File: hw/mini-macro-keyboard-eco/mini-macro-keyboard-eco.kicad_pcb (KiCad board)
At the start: 2 copper layers, 59.2 x 30.5 mm, 32 parts, among them J0 USB, J1 DEBUG_SWD, SW1 SW_Cherry_MX_1.00u_PCB, SW2 SW_Cherry_MX_1.00u_PCB, SW3 SW_Cherry_MX_1.00u_PCB, SW5 LAYOUT, SW6 BACKLIGHT, U1 USBLC6-2SC6, U2 XC6206P322MR, U3 STM32F070F6P6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

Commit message: fix(hw): reroute some traces
Signed-off-by: Ivan Kovalenko <s1ckretbox@gmail.com>
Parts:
- moved C0 4.99 mm to (125.1, 112.6)
- moved C1 4.11 mm to (127.3, 109.9), turned to 0 degrees
- moved R0 2.35 mm to (130.1, 111.4)
- moved Y1 0.54 mm to (127.3, 112.5), turned to 90 degrees
- moved R2 0.09 mm to (143.3, 105.1)
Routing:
- net GND: track 30.6 -> 48.8 mm, vias 10 -> 12
- net Net-(J0-Pad6): track 0.00 -> 12.4 mm
- net USB_D-: track 22.1 -> 27.4 mm
- net USB_D+: track 22.9 -> 28.1 mm
- net OSC_IN: track 4.72 -> 7.76 mm
- net OSC_OUT: track 4.25 -> 1.27 mm
- net +3V3: track 18.2 -> 21.2 mm, vias 4 -> 6
- net Net-(C1-Pad2): track 3.75 -> 3.18 mm
- net SWCLK: vias 0 -> 1

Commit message: fix(hw, #3): remove R0 resistor
Signed-off-by: Ivan Kovalenko <s1ckretbox@gmail.com>
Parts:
- removed R0: 47, Resistor_SMD:R_0402_1005Metric
- moved Y1 2.28 mm to (129.5, 112.0)
- moved C0 2.13 mm to (127.2, 112.6)
- moved C1 1.94 mm to (129.1, 109.2)
- moved C3 1.44 mm to (130.7, 108.6), turned to 90 degrees
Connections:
- C1 pad 2: Net-(C1-Pad2) -> OSC_OUT
- Y1 pad 3: Net-(C1-Pad2) -> OSC_OUT
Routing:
- net GND: track 48.8 -> 42.7 mm, vias 12 -> 11
- net Net-(C1-Pad2): track 3.18 -> 0.00 mm
- net OSC_OUT: track 1.27 -> 4.22 mm
- net OSC_IN: track 7.76 -> 6.25 mm

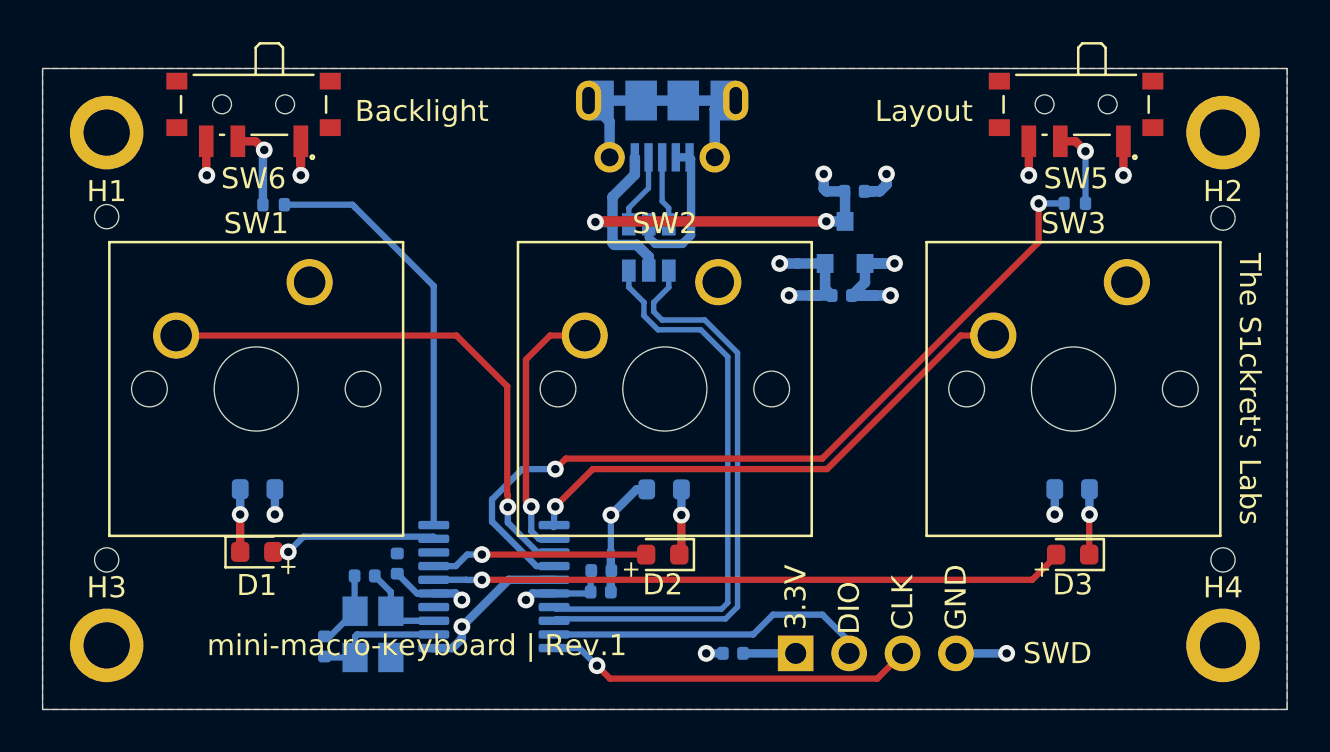
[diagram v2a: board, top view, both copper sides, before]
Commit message: fix(hw, #4): remove 3.3v plate filling
Signed-off-by: Ivan Kovalenko <s1ckretbox@gmail.com>
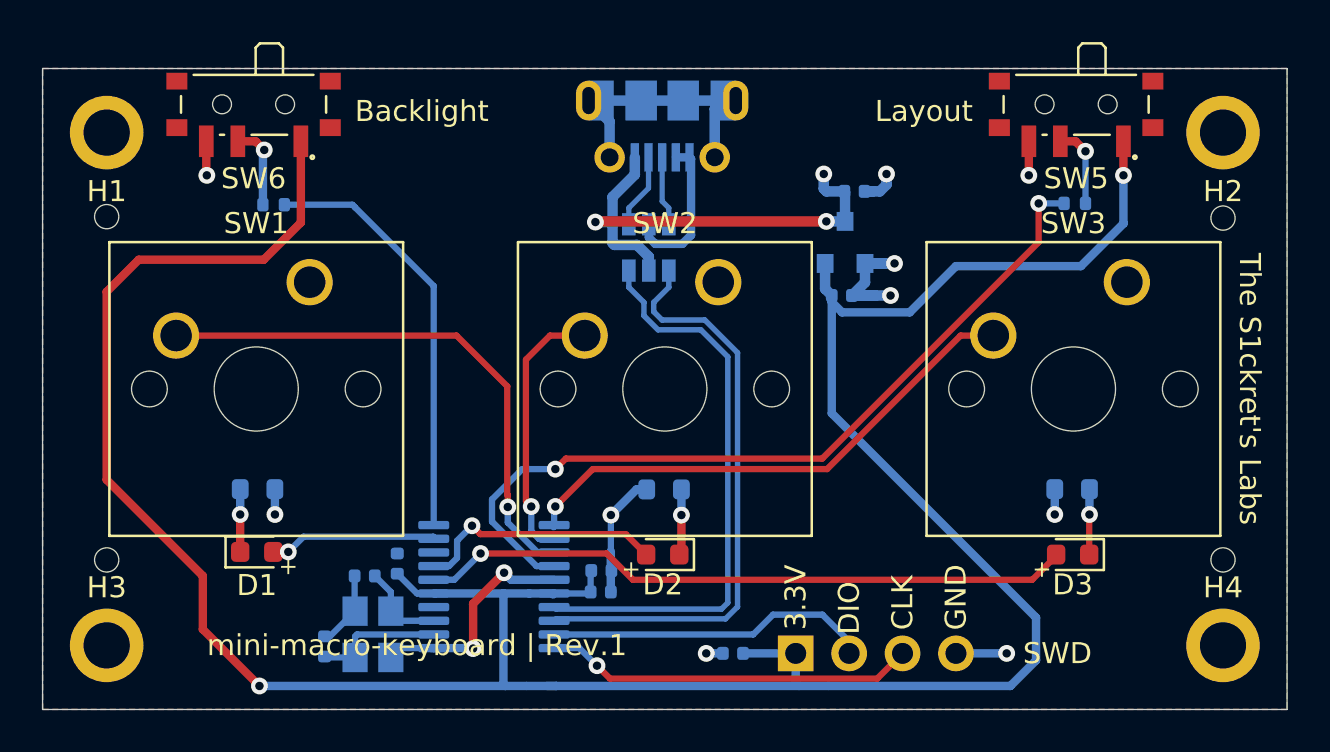
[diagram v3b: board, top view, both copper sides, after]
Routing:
- net +3V3: track 21.5 -> 136.6 mm, vias 6 -> 2
- net GND: track 42.7 -> 46.2 mm, vias 11 -> 12
- net LED_2: track 10.3 -> 11.9 mm
- net LED_3: track 30.2 -> 31.2 mm
- added copper zone on F.Cu, net GND
- removed copper zone on F.Cu, net +3V3
